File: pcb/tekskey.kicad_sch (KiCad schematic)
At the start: 90 parts, among them SW0 MX_SW_HS, SW0B1 MX_SW_HS, SW1 MX_SW_HS, SW10 MX_SW_HS, SW11 MX_SW_HS, SW12 MX_SW_HS, SW13 MX_SW_HS, SW14 MX_SW_HS, SW15 MX_SW_HS, SW1B1 MX_SW_HS, SW2 MX_SW_HS, SW20 MX_SW_HS, SW21 MX_SW_HS, SW22 MX_SW_HS, SW23 MX_SW_HS, SW24 MX_SW_HS, SW25 MX_SW_HS, SW2B1 MX_SW_HS, SW3 MX_SW_HS, SW30 MX_SW_HS, SW31 MX_SW_HS, SW32 MX_SW_HS, SW33 MX_SW_HS, SW34 MX_SW_HS, SW35 MX_SW_HS, SW3B1 MX_SW_HS, SW4 MX_SW_HS, SW40 MX_SW_HS, SW41 MX_SW_HS, SW42 MX_SW_HS, SW43 MX_SW_HS, SW44 MX_SW_HS, SW45 MX_SW_HS, SW4B1 MX_SW_HS, SW5 MX_SW_HS, SW50 MX_SW_HS, SW51 MX_SW_HS, SW52 MX_SW_HS, SW53 MX_SW_HS, SW54 MX_SW_HS, SW55 MX_SW_HS

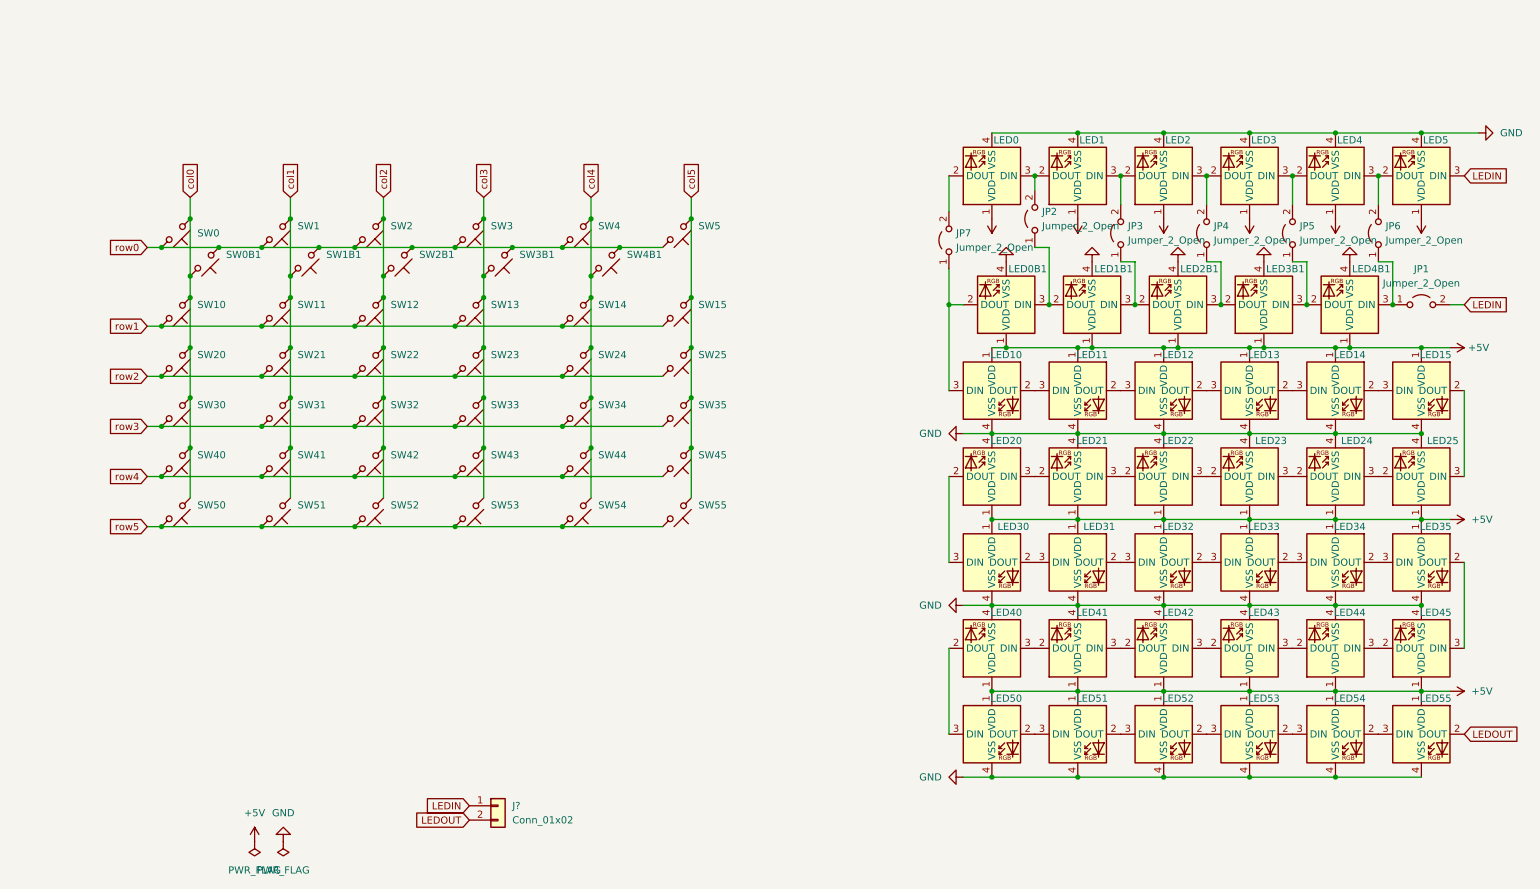
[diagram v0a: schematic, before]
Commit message: rotate each key
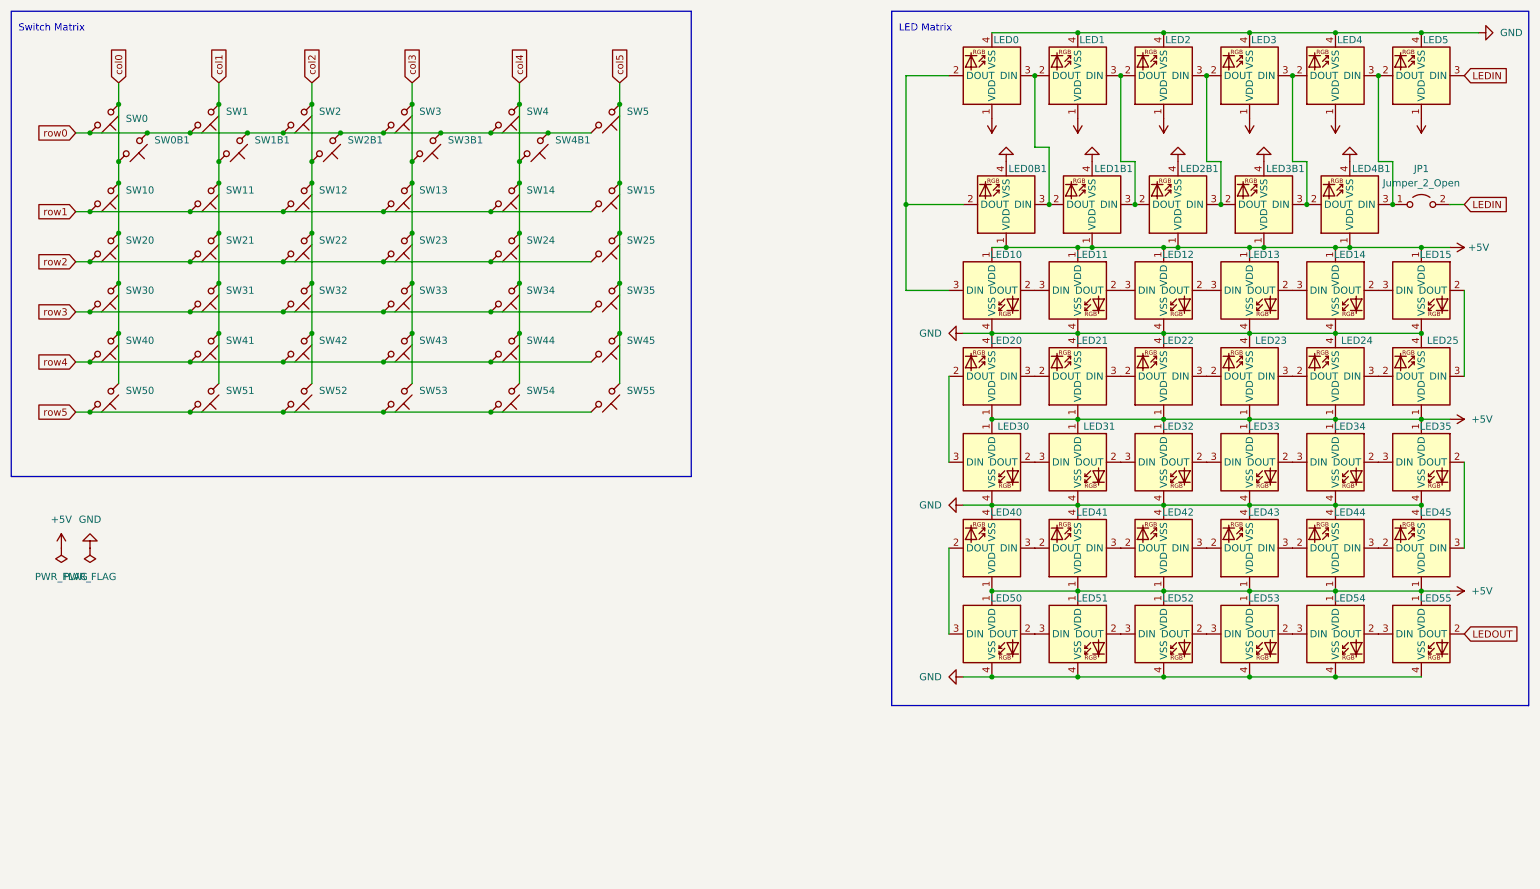
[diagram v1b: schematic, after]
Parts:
- removed J?: Conn_01x02, symbol Connector_Generic:Conn_01x02
- removed JP2, JP3, JP4, JP5, JP6, JP7: Jumper_2_Open, symbol Jumper:Jumper_2_Open
- JP1: footprint (none) -> Jumper:SolderJumper-2_P1.3mm_Open_Pad1.0x1.5mm
- LED0, LED0B1, LED1, LED1B1, LED2, LED20, LED21, LED22, LED23, LED24, LED25, LED2B1, LED3, LED3B1, LED4, LED40, LED41, LED42, LED43, LED44, LED45, LED4B1, LED5: footprint marbastlib-mx:LED_MX_6028R-FLIPPED -> marbastlib-mx:LED_MX_6028R
- LED10, LED11, LED12, LED13, LED14, LED15, LED30, LED31, LED32, LED33, LED34, LED35, LED50, LED51, LED52, LED53, LED54, LED55: footprint marbastlib-mx:LED_MX_6028R -> marbastlib-mx:LED_MX_6028R-FLIPPED
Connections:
- net at LED1B1.3 (DIN), LED2B1.2 (DOUT): now also LED1.3 (DIN), LED2.2 (DOUT)
- net at JP1.1 (A), LED4B1.3 (DIN): now also LED4.3 (DIN), LED5.2 (DOUT)
- net at LED2B1.3 (DIN), LED3B1.2 (DOUT): now also LED2.3 (DIN), LED3.2 (DOUT)
- net at LED0B1.2 (DOUT), LED10.3 (DIN): now also LED0.2 (DOUT)
- net at LED0B1.3 (DIN), LED1B1.2 (DOUT): now also LED0.3 (DIN), LED1.2 (DOUT)
- net at LED3.3 (DIN), LED4.2 (DOUT): now also LED3B1.3 (DIN), LED4B1.2 (DOUT)
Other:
- note added: "LED Matrix"
- note added: "Switch Matrix"
- moved on the sheet: JP1, LED0, LED0B1, LED1, LED10, LED11, LED12, LED13, LED14, LED15, LED1B1, LED2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

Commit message: add led jumper
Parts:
- removed SW0B1: MX_SW_HS, marbastlib-mx:SW_MX_HS_1u, symbol marbastlib-mx:MX_SW_HS
- added JP10, JP11, JP12, JP13, JP14, JP15, JP16, JP17, JP2, JP3, JP4, JP5, JP6, JP7, JP8, JP9: Jumper_2_Open, Jumper:SolderJumper-2_P1.3mm_Open_Pad1.0x1.5mm, symbol Jumper:Jumper_2_Open
- added LED6, LED7: MX_SK6812MINI-E, marbastlib-mx:LED_MX_6028R-FLIPPED, symbol marbastlib-mx:MX_SK6812MINI-E
- added SW51B1, SW55B1, SW5B1: MX_SW_HS, marbastlib-mx:SW_MX_HS_1u, symbol marbastlib-mx:MX_SW_HS
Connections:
- net +5V: now also LED6.1 (VDD), LED7.1 (VDD)
- net GND: now also LED6.4 (VSS), LED7.4 (VSS)
- net LEDOUT: now also JP17.2 (B)
- net col1: now also SW51B1.2
- net col5: now also SW55B1.2, SW5B1.2
- net row0: now also SW5B1.1
- net row5: now also SW51B1.1, SW55B1.1
- net at JP1.1 (A), LED4B1.3 (DIN), LED5.2 (DOUT): now also JP11.2 (B); no longer LED4.3 (DIN)
- net at LED51.2 (DOUT), LED52.3 (DIN): now also JP14.2 (B)
- net at LED50.2 (DOUT): now also JP12.1 (A), JP13.1 (A), LED6.3 (DIN); no longer LED51.3 (DIN)
- net at LED0.2 (DOUT), LED10.3 (DIN): now also JP2.1 (A); no longer LED0B1.2 (DOUT)
- net at LED40.2 (DOUT), LED50.3 (DIN): now also JP12.2 (B)
- net at LED0B1.3 (DIN), LED1.2 (DOUT): now also JP3.2 (B), JP4.1 (A); no longer LED0.3 (DIN), LED1B1.2 (DOUT)
- net at LED1B1.3 (DIN), LED2.2 (DOUT): now also JP5.2 (B), JP6.1 (A); no longer LED1.3 (DIN), LED2B1.2 (DOUT)
- net at LED3B1.3 (DIN), LED4.2 (DOUT): now also JP10.1 (A), JP9.2 (B); no longer LED3.3 (DIN), LED4B1.2 (DOUT)
- net at LED2B1.3 (DIN), LED3.2 (DOUT): now also JP7.2 (B), JP8.1 (A); no longer LED2.3 (DIN), LED3B1.2 (DOUT)
- net at LED53.2 (DOUT), LED54.3 (DIN): now also JP15.1 (A)
- net at LED54.2 (DOUT): now also JP15.2 (B), JP16.1 (A), LED7.3 (DIN); no longer LED55.3 (DIN)
- new net: JP10.2 (B), JP11.1 (A), LED4.3 (DIN), LED4B1.2 (DOUT)
- new net: JP13.2 (B), JP14.1 (A), LED51.3 (DIN), LED6.2 (DOUT)
- new net: JP4.2 (B), JP5.1 (A), LED1.3 (DIN), LED1B1.2 (DOUT)
- new net: JP16.2 (B), JP17.1 (A), LED55.3 (DIN), LED7.2 (DOUT)
- new net: JP2.2 (B), JP3.1 (A), LED0.3 (DIN), LED0B1.2 (DOUT)
- new net: JP8.2 (B), JP9.1 (A), LED3.3 (DIN), LED3B1.2 (DOUT)
- new net: JP6.2 (B), JP7.1 (A), LED2.3 (DIN), LED2B1.2 (DOUT)
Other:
- moved on the sheet: JP1, LED0, LED0B1, LED1, LED11, LED12, LED13, LED14, LED15, LED1B1, LED2, LED21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

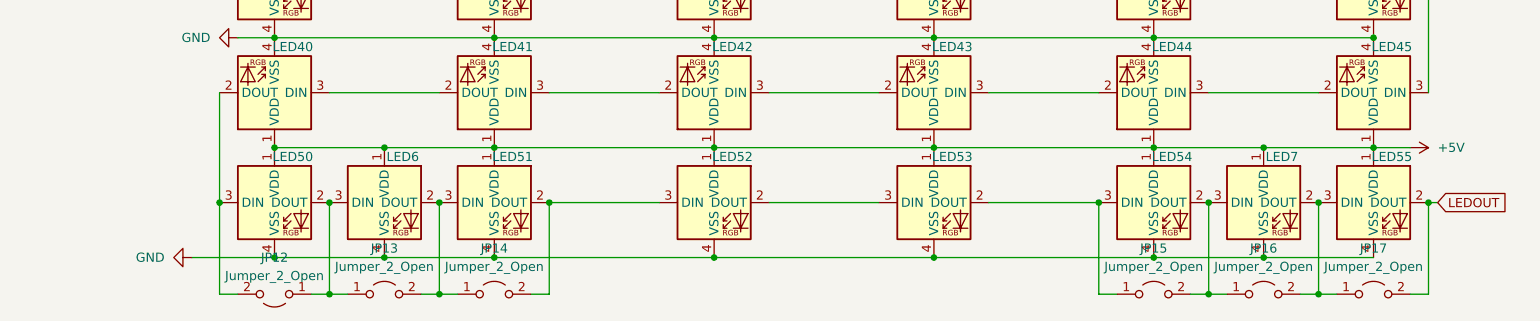
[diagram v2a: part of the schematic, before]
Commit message: remove some jumpers
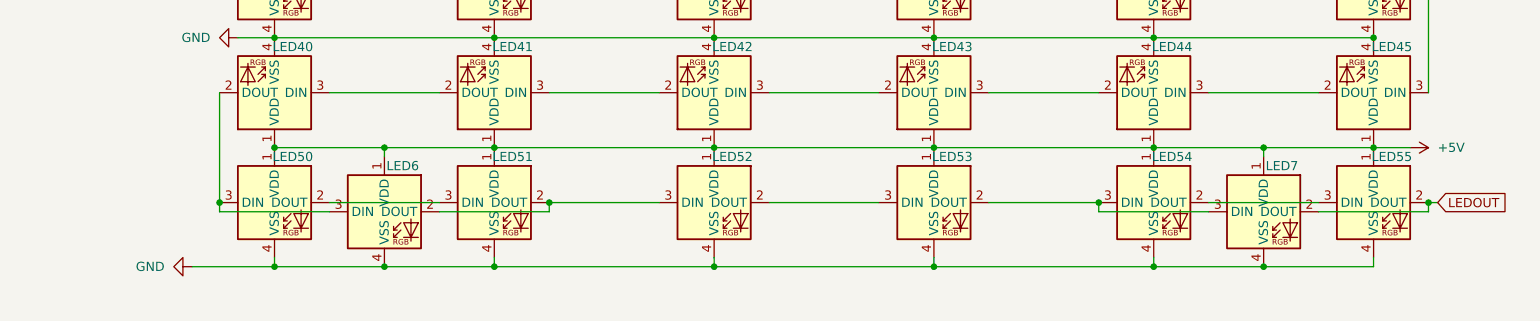
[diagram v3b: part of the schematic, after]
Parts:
- removed JP12, JP13, JP14, JP15, JP16, JP17: Jumper_2_Open, Jumper:SolderJumper-2_P1.3mm_Open_Pad1.0x1.5mm, symbol Jumper:Jumper_2_Open
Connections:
- net LEDOUT: now also LED7.2 (DOUT)
- net at LED53.2 (DOUT), LED54.3 (DIN): now also LED7.3 (DIN)
- net at LED54.2 (DOUT): now also LED55.3 (DIN); no longer LED7.3 (DIN)
- net at LED50.2 (DOUT): now also LED51.3 (DIN); no longer LED6.3 (DIN)
- net at LED40.2 (DOUT), LED50.3 (DIN): now also LED6.3 (DIN)
- net at LED6.2 (DOUT): now also LED51.2 (DOUT), LED52.3 (DIN); no longer LED51.3 (DIN)
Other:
- moved on the sheet: LED6, LED7

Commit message: add through hole diodes
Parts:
- added D1, D10, D11, D12, D13, D14, D15, D16, D17, D18, D19, D2, D20, D21, D22, D23, D24, D25, D26, D27, D28, D29, D3, D30, D31, D32, D33, D34, D35, D36, D4, D5, D6, D7, D8, D9: 1N4148, Diode_THT:D_DO-35_SOD27_P7.62mm_Horizontal, symbol Diode:1N4148
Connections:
- net col0: now also D1.1 (K), D14.1 (K), D19.1 (K), D25.1 (K), D7.1 (K); no longer SW10.1, SW20.1, SW30.1, SW40.1, SW50.1
- net col1: now also D15.1 (K), D2.1 (K), D20.1 (K), D26.1 (K), D8.1 (K); no longer SW11.1, SW21.1, SW31.1, SW41.1, SW51.1, SW51B1.2
- net col2: now also D13.1 (K), D21.1 (K), D27.1 (K), D3.1 (K), D9.1 (K); no longer SW12.1, SW22.1, SW32.1, SW42.1, SW52.1
- net col3: now also D10.1 (K), D16.1 (K), D22.1 (K), D28.1 (K), D4.1 (K); no longer SW13.1, SW23.1, SW33.1, SW43.1, SW53.1
- net col4: now also D11.1 (K), D17.1 (K), D23.1 (K), D29.1 (K), D5.1 (K); no longer SW14.1, SW24.1, SW34.1, SW44.1, SW54.1
- net col5: now also D12.1 (K), D18.1 (K), D24.1 (K), D30.1 (K), D6.1 (K); no longer SW15.1, SW25.1, SW35.1, SW45.1, SW55.1, SW55B1.2
- net row0: now also D31.2 (A), D32.2 (A), D33.2 (A), D34.2 (A), D35.2 (A), D36.2 (A); no longer SW0.2, SW1.2, SW1B1.1, SW2.2, SW2B1.1, SW3.2, SW3B1.1, SW4.2, SW4B1.1, SW5.2, SW5B1.1
- net row5: now also SW51B1.2, SW55B1.2; no longer SW51B1.1, SW55B1.1
- new net: D35.1 (K), SW4.2, SW4B1.1
- new net: D31.1 (K), SW0.2
- new net: D32.1 (K), SW1.2, SW1B1.1
- new net: D25.2 (A), SW50.1
- new net: D28.2 (A), SW53.1
- new net: D16.2 (A), SW33.1
- new net: D29.2 (A), SW54.1
- new net: D6.2 (A), SW15.1
- new net: D18.2 (A), SW35.1
- new net: D22.2 (A), SW43.1
- new net: D30.2 (A), SW55.1, SW55B1.1
- new net: D17.2 (A), SW34.1
- new net: D5.2 (A), SW14.1
- new net: D13.2 (A), SW32.1
- new net: D14.2 (A), SW30.1
- new net: D9.2 (A), SW22.1
- new net: D20.2 (A), SW41.1
- new net: D36.1 (K), SW5.2, SW5B1.1
- new net: D15.2 (A), SW31.1
- new net: D23.2 (A), SW44.1
- new net: D26.2 (A), SW51.1, SW51B1.1
- new net: D4.2 (A), SW13.1
- new net: D10.2 (A), SW23.1
- new net: D12.2 (A), SW25.1
- new net: D7.2 (A), SW20.1
- new net: D24.2 (A), SW45.1
- new net: D33.1 (K), SW2.2, SW2B1.1
- new net: D34.1 (K), SW3.2, SW3B1.1
- new net: D19.2 (A), SW40.1
- new net: D8.2 (A), SW21.1
- new net: D2.2 (A), SW11.1
- new net: D21.2 (A), SW42.1
- new net: D1.2 (A), SW10.1
- new net: D11.2 (A), SW24.1
- new net: D27.2 (A), SW52.1
- new net: D3.2 (A), SW12.1
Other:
- moved on the sheet: JP1, JP10, JP11, JP2, JP3, JP4, JP5, JP6, JP7, JP8, JP9, LED0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

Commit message: align switches
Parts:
- added J1, J2: Conn_01x08, Connector_PinHeader_2.54mm:PinHeader_1x08_P2.54mm_Vertical, symbol Connector_Generic:Conn_01x08
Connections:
- net col0: now also J2.1 (Pin_1)
- net col1: now also J2.2 (Pin_2)
- net col2: now also J2.3 (Pin_3)
- net col3: now also J2.4 (Pin_4)
- net col4: now also J2.5 (Pin_5)
- net col5: now also J2.6 (Pin_6)
- net row0: now also J1.1 (Pin_1)
- net row1: now also J1.2 (Pin_2)
- net row2: now also J1.3 (Pin_3)
- net row3: now also J1.4 (Pin_4)
- net row4: now also J1.5 (Pin_5)
- net row5: now also J1.6 (Pin_6)
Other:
- moved on the sheet: D1, D10, D11, D12, D13, D14, D15, D16, D17, D18, D19, D2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

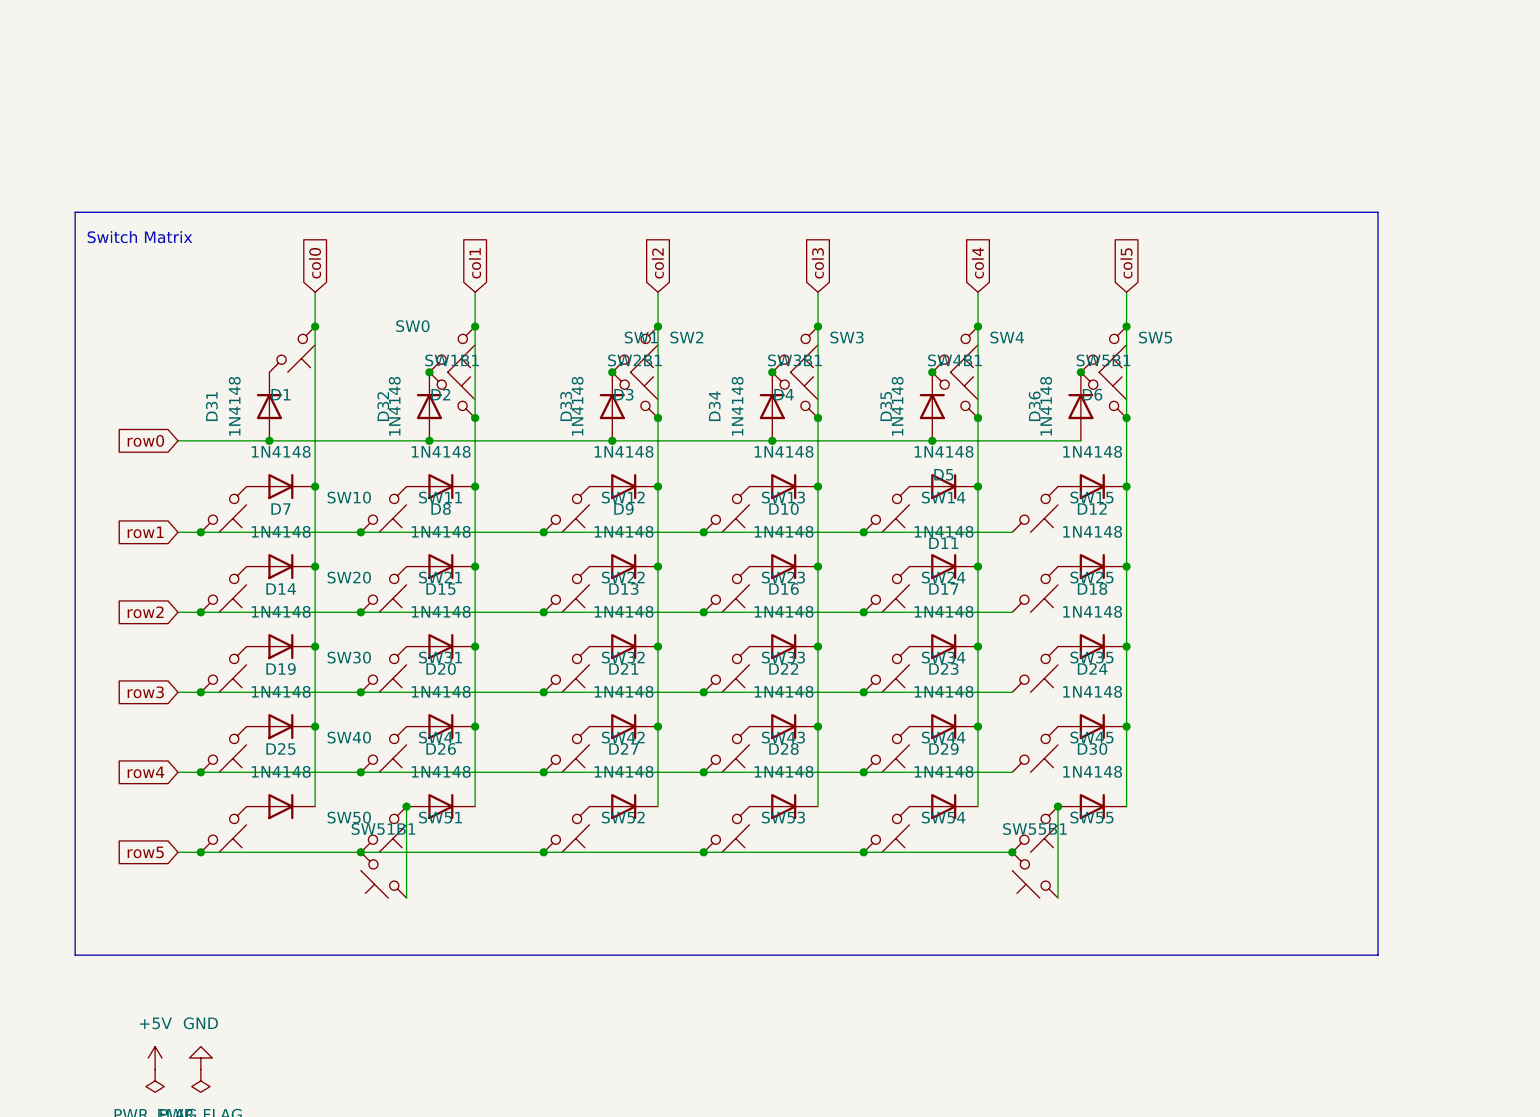
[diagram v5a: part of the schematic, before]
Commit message: fix diode assignment
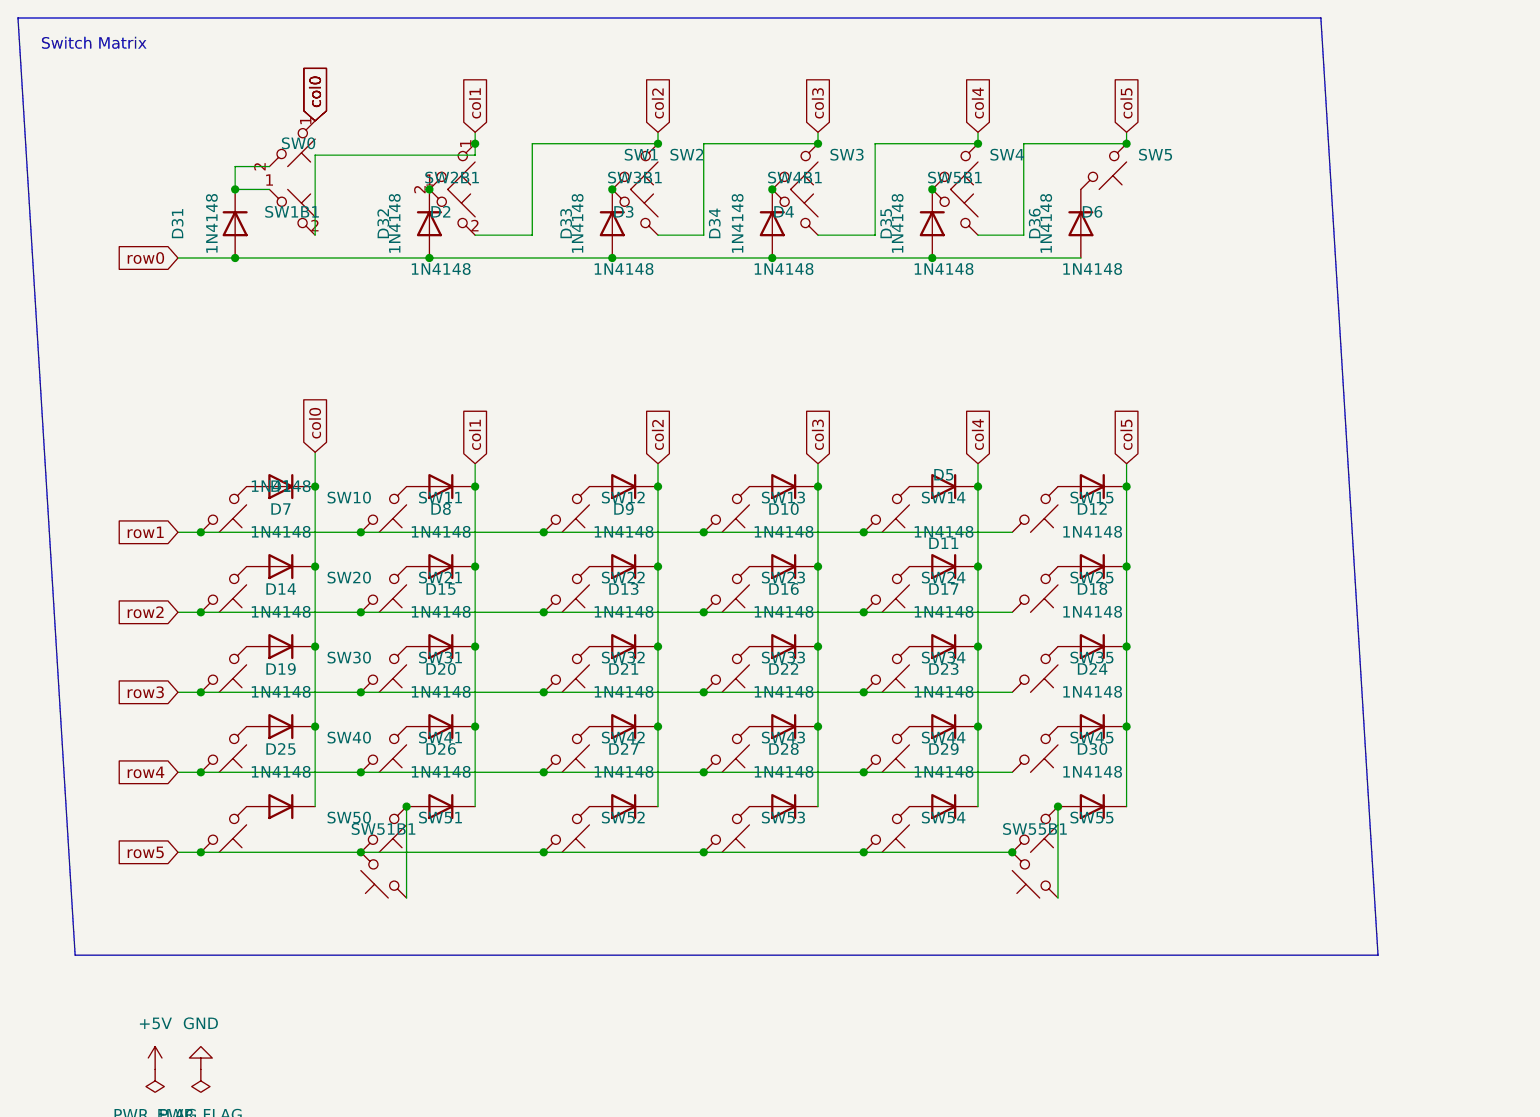
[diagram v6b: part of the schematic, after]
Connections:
- net at D35.1 (K), SW4.2: now also SW5B1.1; no longer SW4B1.1
- net at D31.1 (K), SW0.2: now also SW1B1.1
- net at D32.1 (K), SW1.2: now also SW2B1.1; no longer SW1B1.1
- net at D36.1 (K), SW5.2: no longer SW5B1.1
- net at D33.1 (K), SW2.2: now also SW3B1.1; no longer SW2B1.1
- net at D34.1 (K), SW3.2: now also SW4B1.1; no longer SW3B1.1
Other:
- moved on the sheet: D31, D32, D33, D34, D35, D36, SW2, SW3, SW3B1, SW4, SW4B1, SW5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
